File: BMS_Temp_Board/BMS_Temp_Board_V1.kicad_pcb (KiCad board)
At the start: 4 copper layers, 190.5 x 74.1 mm, 87 parts, among them IC1 ESP32-S3-WROOM-1-N8R8, IC10 CD74HC4067PWR, IC11 CD74HC4067PWR, IC12 CD74HC4067PWR, IC13 CD74HC4067PWR, IC14 CD74HC4067PWR, IC15 CD74HC4067PWR, IC2 CP2102N-A02-GQFN28, IC3 TLP175A_TPL,E, IC4 TPS2116DRLR, IC5 MIC37100-3.3WS, IC6 CD74HC4067PWR, IC7 CD74HC4067PWR, IC8 CD74HC4067PWR, IC9 CD74HC4067PWR, J1 ESP_USB, J10 B32B-PUDSS-1_LF__SN_, J11 B32B-PUDSS-1_LF__SN_, J12 B2B-PH-K-S, J14 B2B-PH-K-S, J15 B2B-PH-K-S, J2 B32B-PUDSS-1_LF__SN_, J3 B32B-PUDSS-1_LF__SN_, J4 B32B-PUDSS-1_LF__SN_, J5 B32B-PUDSS-1_LF__SN_, J6 B32B-PUDSS-1_LF__SN_, J7 B32B-PUDSS-1_LF__SN_, J8 B32B-PUDSS-1_LF__SN_, J9 B32B-PUDSS-1_LF__SN_, Q1 MMBT2222LT1G, Q2 MMBT2222LT1G, U1 USBLC6-2SC6, U2 SN65HVD230, U3 LM2575HVS-5.0_NOPB

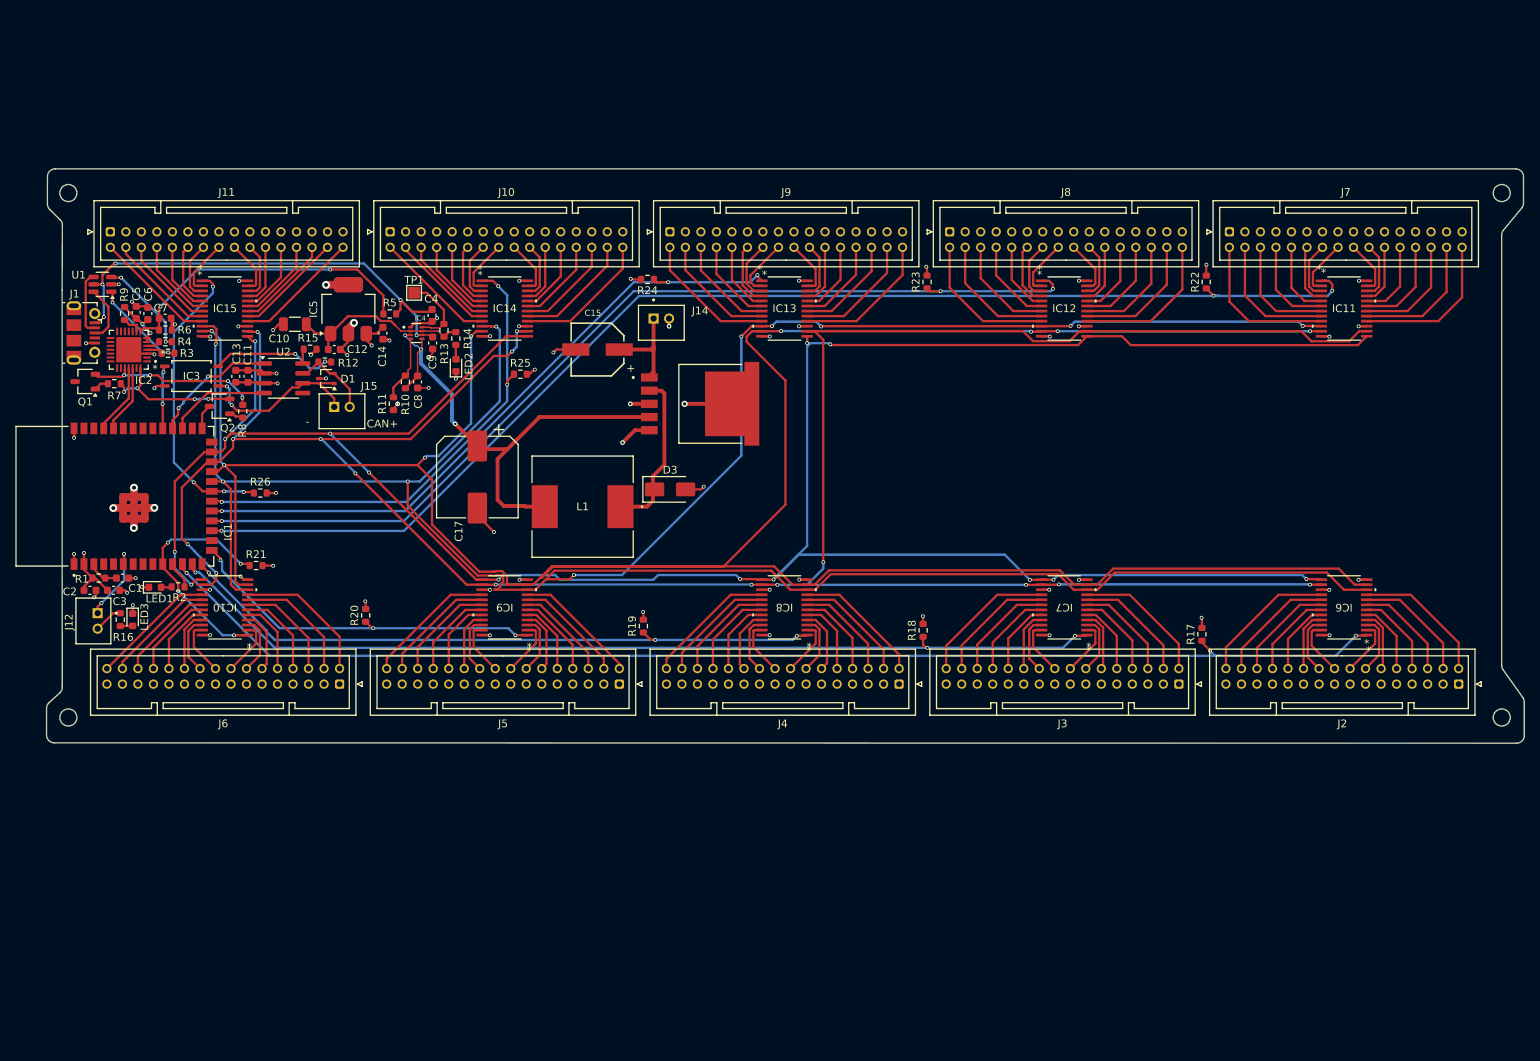
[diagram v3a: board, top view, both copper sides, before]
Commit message: Redesigned BMS Temp Board for 64 thermistors
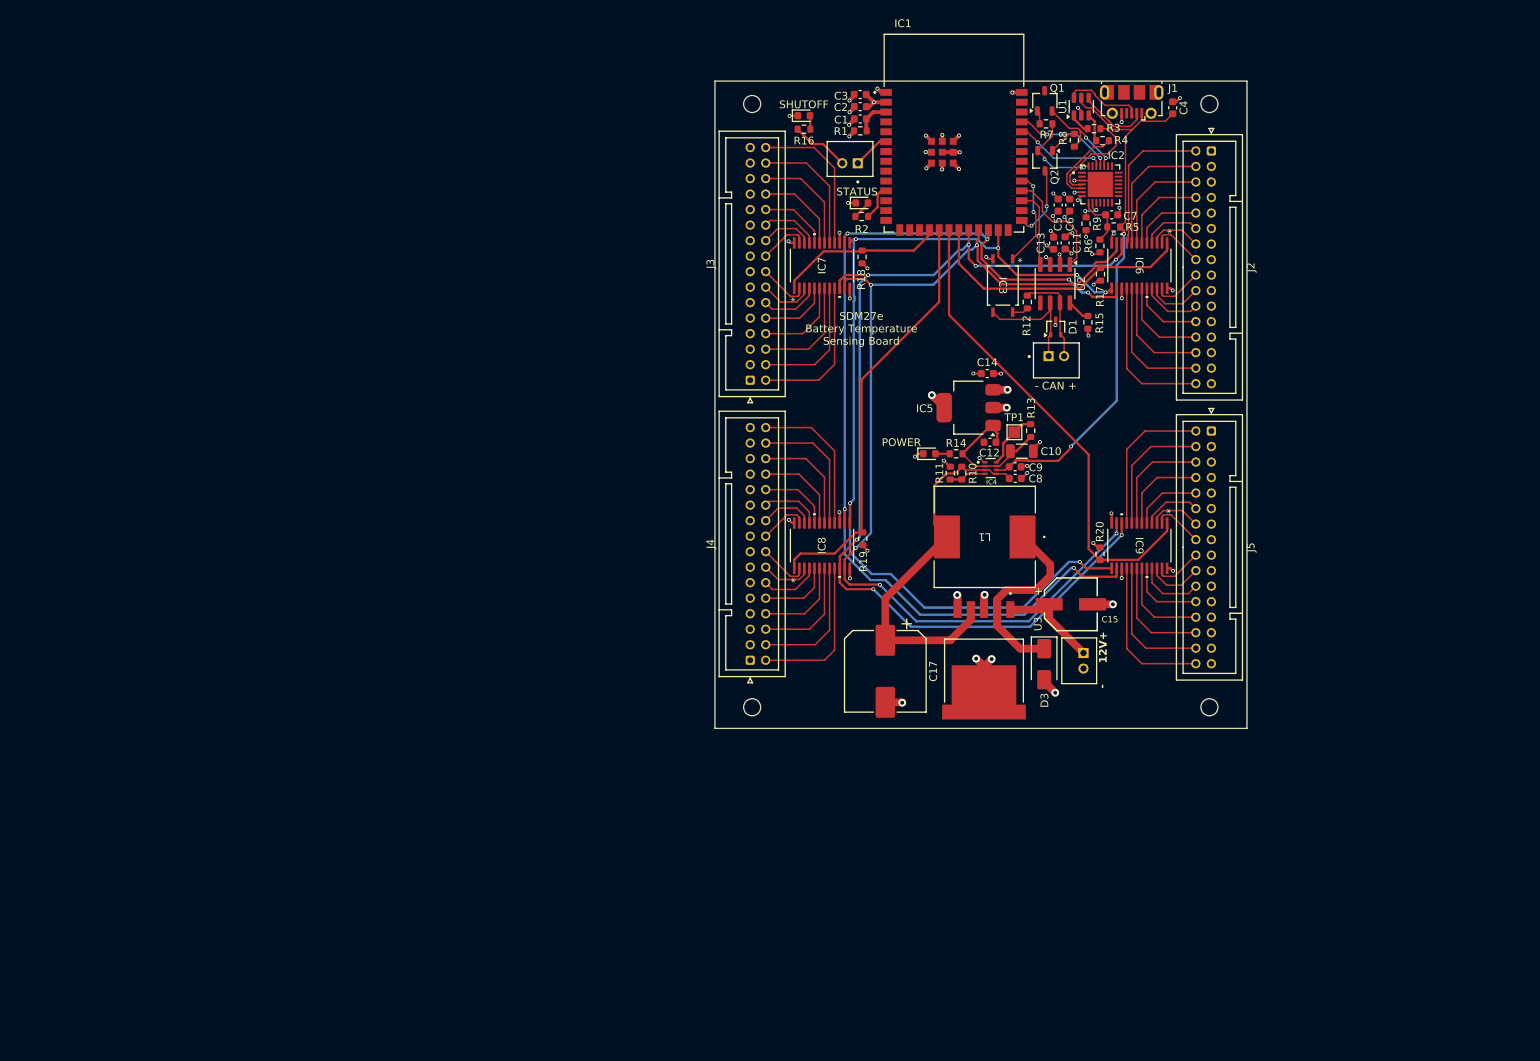
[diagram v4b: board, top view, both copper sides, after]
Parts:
- removed IC10, IC11, IC12, IC13, IC14, IC15: CD74HC4067PWR, CD74HC4067PWR:TSSOP24_4P5X7P9_TEX
- removed J10, J11, J6, J7, J8, J9: B32B-PUDSS-1_LF__SN_, ESP32_S3_WROOM_1_N8R8:JST_PUD_B32B-PUDSS_2x16_P2.00mm_Vertical_PN
- removed J15: B2B-PH-K-S, B2B_PH_K_S:JST_B2B-PH-K-S
- removed LED1: GREEN, LED_SMD:LED_0603_1608Metric
- removed LED2: 150060RS75000, LED_SMD:LED_0603_1608Metric
- removed LED3: LED, LED_SMD:LED_0603_1608Metric
- removed R21, R22, R23, R24, R25, R26: 10k, Resistor_SMD:R_0603_1608Metric
- added - CAN +: B2B-PH-K-S, B2B_PH_K_S:JST_B2B-PH-K-S, F.Cu at (177.9, 87.4)
- added POWER: 150060RS75000, LED_SMD:LED_0603_1608Metric, F.Cu at (161.6, 99.4)
- added SHUTOFF: LED, LED_SMD:LED_0603_1608Metric, F.Cu at (145.4, 55.9)
- added STATUS: GREEN, LED_SMD:LED_0603_1608Metric, F.Cu at (152.9, 67.1)
- moved H3 147.1 mm to (197.7, 132.1)
- moved J1 138.4 mm to (187.7, 54.1), turned to 180 degrees
- moved Q1 128.9 mm to (176.4, 53.9), turned to 90 degrees
- moved U1 128.3 mm to (181.2, 54.7), turned to 90 degrees
- moved IC2 127.1 mm to (183.6, 64.7), turned to 0 degrees
- moved H2 124.9 mm to (138.7, 54.3)
- moved R7 124.7 mm to (176.6, 56.9)
- moved R9 124.5 mm to (181.8, 69.8), turned to -90 degrees
- moved R4 123.6 mm to (183.9, 59.1), turned to 180 degrees
- moved R3 122.9 mm to (182.8, 57.5), turned to 0 degrees
- moved C7 122.8 mm to (185.1, 68.6)
- moved R6 121.0 mm to (183.6, 72.6), turned to -90 degrees
- moved C5 119.7 mm to (178.2, 67.4), turned to -90 degrees
- moved C6 119.7 mm to (179.7, 67.4), turned to 90 degrees
- moved IC1 117.9 mm to (164.7, 58.1), turned to 0 degrees
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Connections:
- IC1 pad 10: /MUX5 -> unconnected-(IC1-IO17-Pad10)
- IC1 pad 12: /MUX1 -> unconnected-(IC1-IO8-Pad12)
- IC1 pad 13: /MUX2 -> unconnected-(IC1-IO19-Pad13)
- IC1 pad 14: /MUX3 -> unconnected-(IC1-IO20-Pad14)
- IC1 pad 15: /MUX4 -> unconnected-(IC1-IO3-Pad15)
- IC1 pad 17: /MUX6 -> unconnected-(IC1-IO9-Pad17)
- IC1 pad 18: /MUX7 -> /MUX2
- IC1 pad 19: /MUX8 -> /MUX3
- IC1 pad 20: /MUX9 -> /MUX4
- IC1 pad 21: /MUX10 -> /MUX1
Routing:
- net /MUX_S1: track 357.5 -> 129.6 mm, vias 8 -> 5
- net /MUX_S0: track 354.5 -> 131.7 mm, vias 10 -> 7
- net /MUX_S3: track 332.4 -> 122.8 mm, vias 14 -> 6
- net /MUX_S2: track 333.4 -> 130.0 mm, vias 15 -> 6
- net /MUX6: track 162.0 -> 0.00 mm, vias 3 -> 0
- net /MUX1: track 162.5 -> 35.5 mm, vias 3 -> 0
- net /MUX7: track 125.0 -> 0.00 mm, vias 3 -> 0
- net /MUX2: track 122.6 -> 21.5 mm, vias 3 -> 0
- net /MUX8: track 85.9 -> 0.00 mm, vias 3 -> 0
- net /MUX9: track 62.9 -> 0.00 mm, vias 3 -> 0
- net GND: track 122.8 -> 78.5 mm, vias 67 -> 57
- net /MUX10: track 38.6 -> 0.00 mm, vias 4 -> 0
- net Net-(IC2-VBUS): track 40.2 -> 7.17 mm, vias 2 -> 0
- net /MUX5: track 30.7 -> 0.00 mm, vias 4 -> 0
- net /MUX3: track 84.5 -> 54.4 mm, vias 3 -> 0
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- added copper zone on In2.Cu, net +3.3V
- added copper zone on In1.Cu, net GND
- removed copper zone on In1.Cu, net +3.3V
- removed copper zone on In2.Cu, net GND
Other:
- board size 190.5 x 74.1 mm -> 68.6 x 83.5 mm
- board text added: "*"
- board text added: "12V+"
- board text added: "SDM27e Battery Temperature Sensing Board"
- board text removed: "CAN+"

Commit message: Changed temp board to use ampseal connector
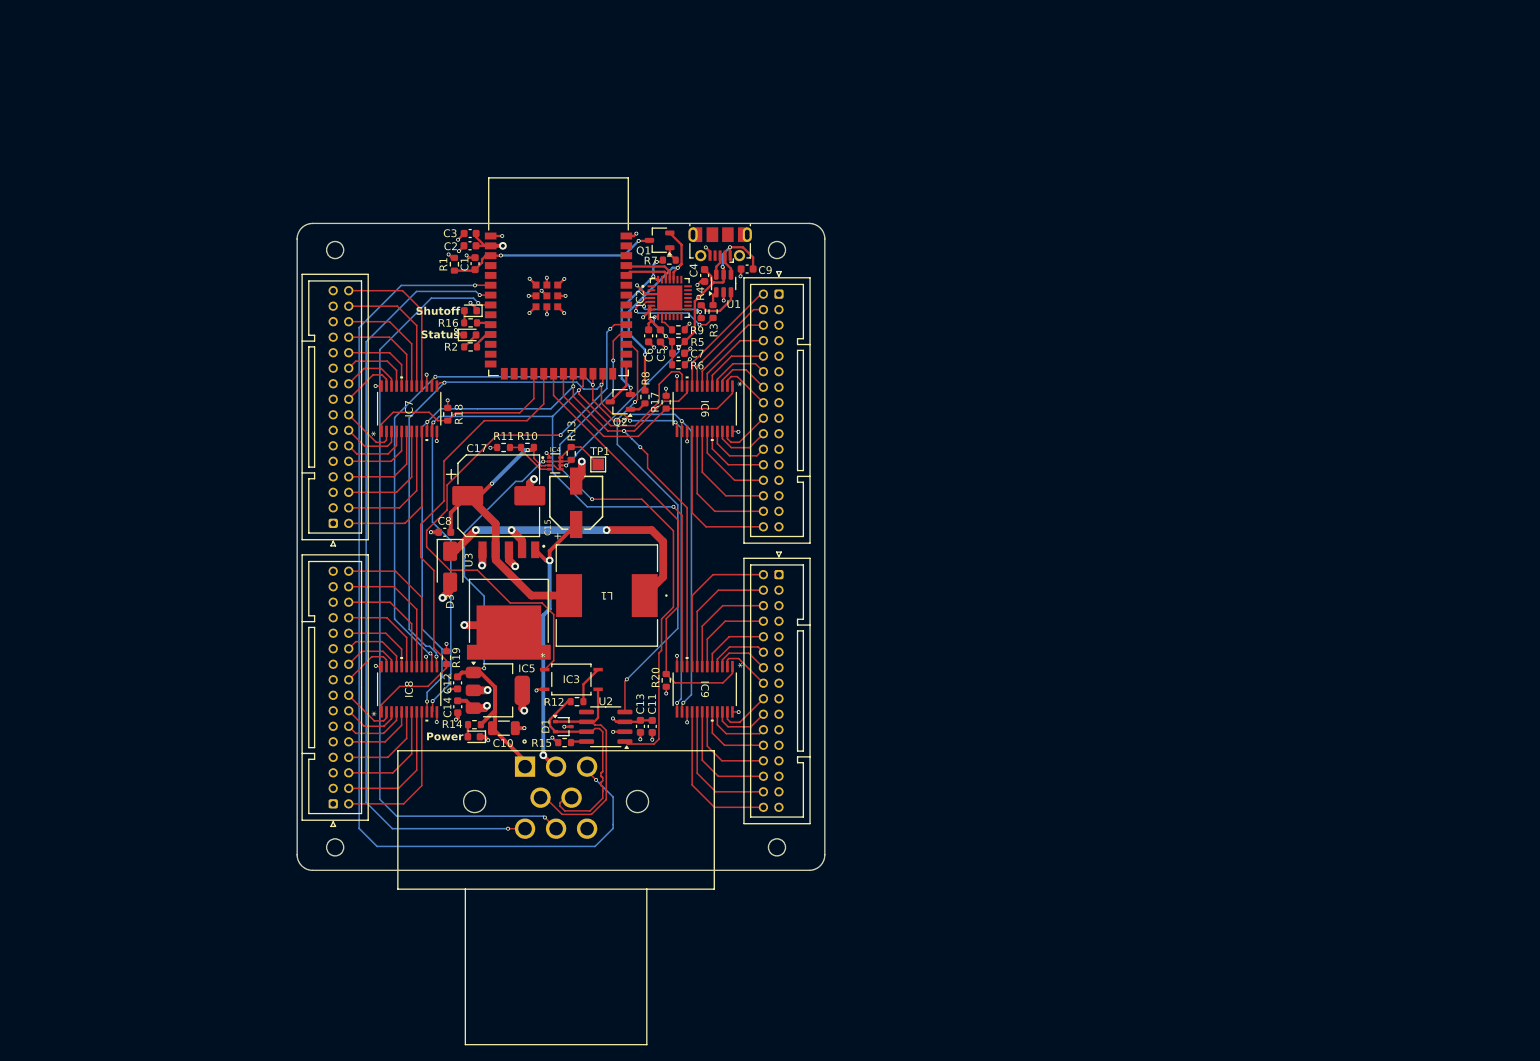
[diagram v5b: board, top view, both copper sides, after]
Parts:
- removed - CAN +: B2B-PH-K-S, B2B_PH_K_S:JST_B2B-PH-K-S
- removed J12, J14: B2B-PH-K-S, B2B_PH_K_S:JST_B2B-PH-K-S
- removed POWER: 150060RS75000, LED_SMD:LED_0603_1608Metric
- removed SHUTOFF: LED, LED_SMD:LED_0603_1608Metric
- removed STATUS: GREEN, LED_SMD:LED_0603_1608Metric
- added J6: 776279-1, 776279_1:TE_776279-1, F.Cu at (113.4, 143.8)
- added LED1: GREEN, LED_SMD:LED_0603_1608Metric, F.Cu at (102.3, 84.1)
- added LED2: 150060RS75000, LED_SMD:LED_0603_1608Metric, F.Cu at (102.8, 135.9)
- added LED3: RED, LED_SMD:LED_0603_1608Metric, F.Cu at (102.4, 81.0)
- moved H1 114.3 mm to (84.9, 73.2)
- moved H2 109.9 mm to (84.9, 150.2)
- moved R15 86.5 mm to (114.5, 136.7), turned to 0 degrees
- moved C11 82.0 mm to (125.8, 134.6), turned to -90 degrees
- moved C13 82.0 mm to (124.3, 134.6), turned to -90 degrees
- moved D1 81.8 mm to (114.4, 134.6), turned to 0 degrees
- moved U2 81.4 mm to (119.8, 134.6), turned to 180 degrees
- moved H3 81.1 mm to (141.9, 73.2)
- moved C14 80.7 mm to (100.8, 132.1), turned to 90 degrees
- moved R12 77.6 mm to (116.1, 131.4), turned to 180 degrees
- moved D3 77.6 mm to (99.8, 114.0)
- moved C10 75.7 mm to (106.7, 134.8)
- moved IC3 75.3 mm to (115.4, 128.5), turned to 0 degrees
- moved C12 75.3 mm to (100.7, 129.0), turned to 90 degrees
- moved C8 73.9 mm to (99.1, 109.6), turned to 0 degrees
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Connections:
- IC1 pad 10: unconnected-(IC1-IO17-Pad10) -> /SHUTDOWN_IND
- IC1 pad 7: unconnected-(IC1-IO7-Pad7) -> /IO7
- IC1 pad 8: unconnected-(IC1-IO15-Pad8) -> /IO15
- Q1 pad 3: unconnected-(Q1-C-Pad3) -> /CHIP_PU
- R16 pad 1: Net-(J12-Pad2) -> /SHUTDOWN_IND
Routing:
- net /SHUTOFF: track 4.81 -> 127.8 mm, vias 0 -> 2
- net /IO7: track 0.00 -> 100.2 mm, vias 0 -> 2
- net /IO15: track 0.00 -> 99.7 mm, vias 0 -> 2
- net /CAN_TERM: track 12.5 -> 72.6 mm
- net /CAN_RTX: track 14.6 -> 71.6 mm, vias 0 -> 2
- net /CAN_CTX: track 10.0 -> 55.4 mm, vias 0 -> 2
- net +5V: track 19.2 -> 61.4 mm, vias 0 -> 2
- net VBUS: track 71.3 -> 46.7 mm, vias 2 -> 4
- net +12V: track 13.4 -> 36.2 mm, vias 0 -> 2
- net /CHIP_PU: track 4.48 -> 27.0 mm, vias 0 -> 2
- net /CAN+: track 12.5 -> 29.6 mm
- net /CAN-: track 16.2 -> 31.5 mm
- net Net-(D3-K): track 25.3 -> 40.3 mm, vias 0 -> 3
- net Net-(IC2-RTS): track 13.1 -> 27.5 mm
- net /MUX_S0: track 131.7 -> 117.6 mm, vias 7 -> 5
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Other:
- board size 68.6 x 83.5 mm -> 68 x 83.4 mm
- board text added: "Power"
- board text added: "Shutoff"
- board text added: "Status"
- board text removed: "*"
- board text removed: "-"
- board text removed: "12V+"
- board text removed: "SDM27e Battery Temperature Sensing Board"

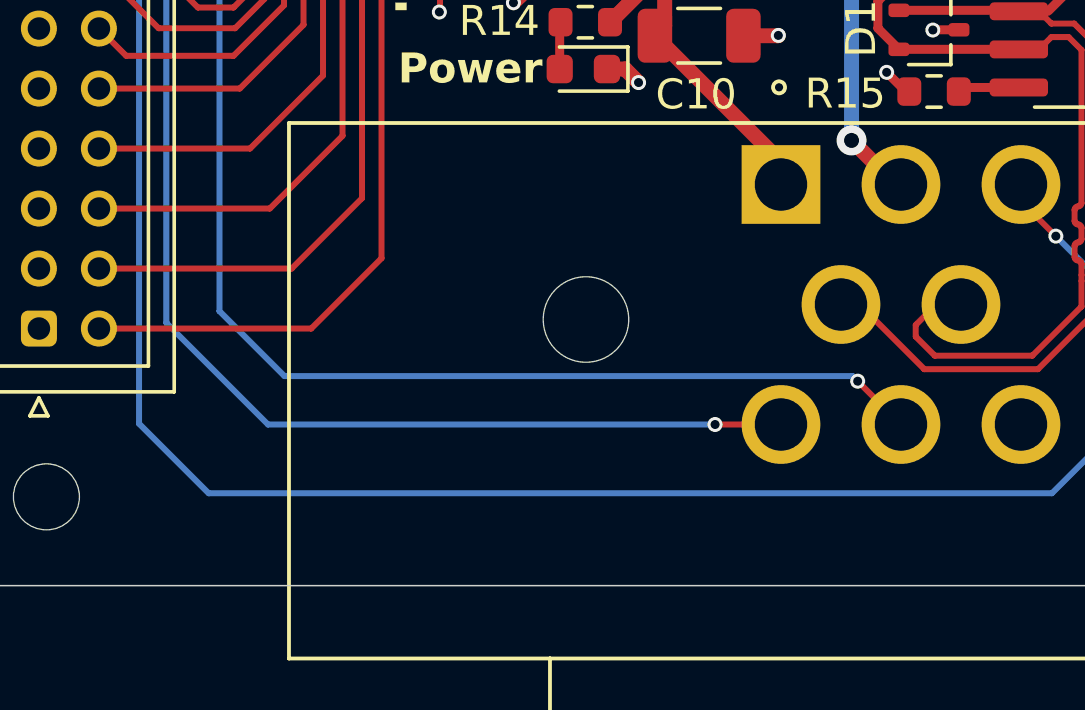
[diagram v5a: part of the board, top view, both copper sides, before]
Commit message: Added Orion input to temp board
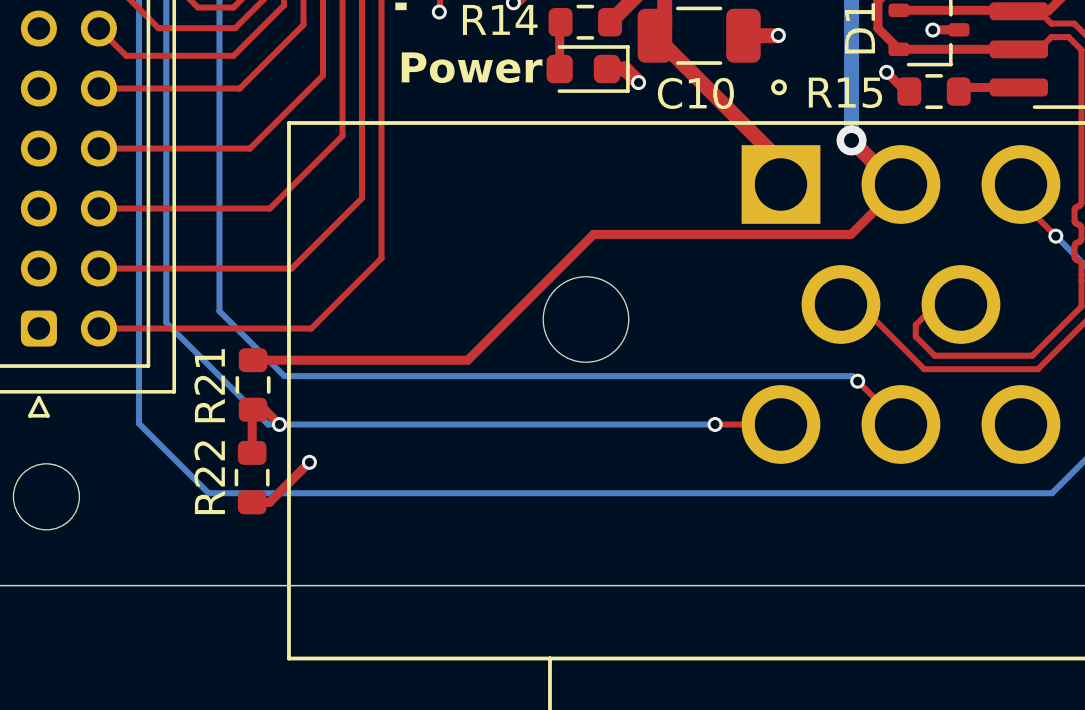
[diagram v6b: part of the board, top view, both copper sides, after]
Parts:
- added R21: 10k, Resistor_SMD:R_0603_1608Metric, F.Cu at (91.8, 146.5)
- added R22: 3.3k, Resistor_SMD:R_0603_1608Metric, F.Cu at (91.8, 149.6)
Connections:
- net /IO7 renamed /ORION
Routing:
- net +12V: track 36.2 -> 60.2 mm
- net /ORION: track 100.2 -> 102.8 mm, vias 2 -> 3
- net GND: track 82.2 -> 84.7 mm, vias 58 -> 59
